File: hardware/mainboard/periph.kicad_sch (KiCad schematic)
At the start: 88 parts, among them J1 Micro_SD_Card_Det, P1 M2_SOCKET_E, Q1 BSS138, Q2 BSS138, Q3 BSS138, Q5 BSS138, Q7 BSS138, SW2 SW_Push, SW3 SW_Push, SW4 SW_Push, SW5 SW_Push, SW6 SW_Push, U10 MMC5983MA, U11 Si52112-B, U21 74LVC2T45DC, U8 TXS02612, U9 ICM-20789, Y1 25MHz

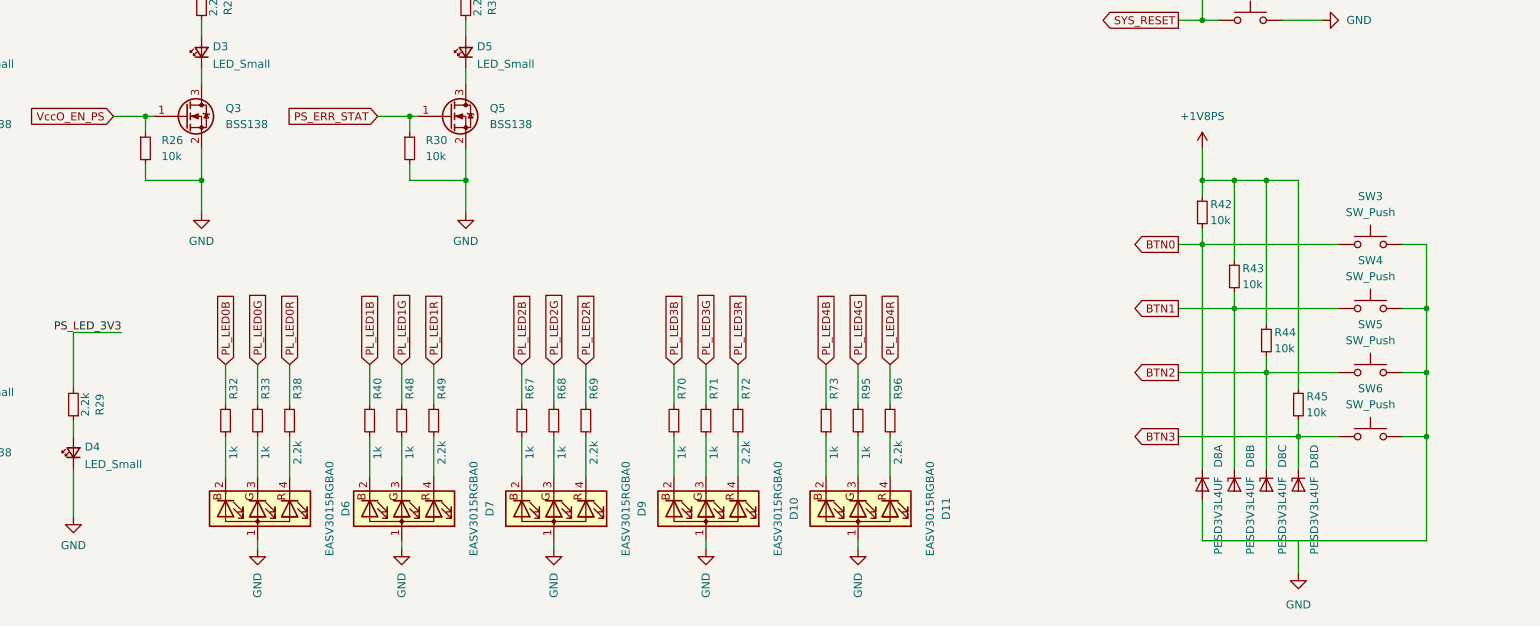
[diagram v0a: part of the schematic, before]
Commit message: Routing various remaining bits
Signed-off-by: gatecat <gatecat@ds0.me>
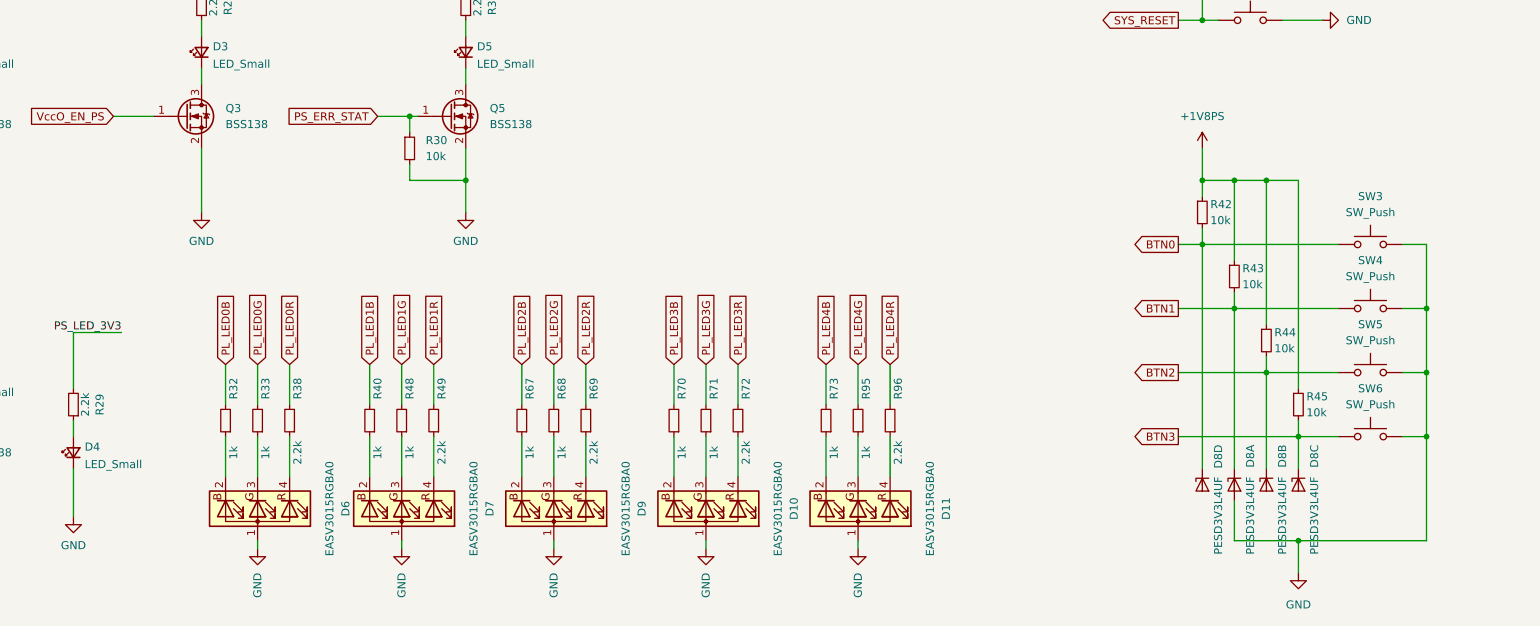
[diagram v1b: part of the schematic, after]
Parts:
- removed R26: 10k, Resistor_SMD:R_0402_1005Metric, symbol Device:R_Small
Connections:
- net BTN0: now also D8.6 (K4); no longer D8.1 (K1)
- net BTN1: now also D8.1 (K1); no longer D8.3 (K2)
- net BTN2: now also D8.3 (K2); no longer D8.4 (K3)
- net BTN3: now also D8.4 (K3); no longer D8.6 (K4)
- net GND: now also D8.2 (A), D8.5 (A), SW3.2, SW4.2, SW5.2, SW6.2
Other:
- moved on the sheet: D8A, D8B, D8C, D8D
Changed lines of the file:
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@@
   (junction (at 218.44 109.22) (diameter 0) (color 0 0 0 0)
   )
-  (junction (at 86.36 215.9) (diameter 0) (color 0 0 0 0)
-  )
   (junction (at 69.85 113.03) (diameter 0) (color 0 0 0 0)
   )
+  (junction (at 260.35 273.05) (diameter 0) (color 0 0 0 0)
+  )
   (junction (at 36.83 257.81) (diameter 0) (color 0 0 0 0)
   )
@@
   (junction (at 226.06 140.97) (diameter 0) (color 0 0 0 0)
   )
-  (junction (at 77.47 205.74) (diameter 0) (color 0 0 0 0)
-  )
   (junction (at 337.82 152.4) (diameter 0) (color 0 0 0 0)
   )
@@
     (stroke (width 0) (type default) (color 0 0 0 0))
   )
+  (wire (pts (xy 250.19 273.05) (xy 260.35 273.05))
+    (stroke (width 0) (type default) (color 0 0 0 0))
+  )
   (wire (pts (xy 140.97 114.3) (xy 140.97 116.84))
     (stroke (width 0) (type default) (color 0 0 0 0))
@@
     (stroke (width 0) (type default) (color 0 0 0 0))
   )
-  (wire (pts (xy 86.36 215.9) (xy 86.36 220.98))
+  (wire (pts (xy 86.36 210.82) (xy 86.36 220.98))
     (stroke (width 0) (type default) (color 0 0 0 0))
   )
@@
     (stroke (width 0) (type default) (color 0 0 0 0))
   )
-  (wire (pts (xy 260.35 273.05) (xy 260.35 278.13))
-    (stroke (width 0) (type default) (color 0 0 0 0))
-  )
   (wire (pts (xy 69.85 78.74) (xy 77.47 78.74))
     (stroke (width 0) (type default) (color 0 0 0 0))
@@
     (stroke (width 0) (type default) (color 0 0 0 0))
   )
-  (wire (pts (xy 77.47 208.28) (xy 77.47 205.74))
-    (stroke (width 0) (type default) (color 0 0 0 0))
-  )
   (wire (pts (xy 241.3 129.54) (xy 241.3 127))
     (stroke (width 0) (type default) (color 0 0 0 0))
@@
     (stroke (width 0) (type default) (color 0 0 0 0))
   )
-  (wire (pts (xy 245.11 266.7) (xy 245.11 273.05))
-    (stroke (width 0) (type default) (color 0 0 0 0))
-  )
   (wire (pts (xy 280.67 273.05) (xy 280.67 256.54))
     (stroke (width 0) (type default) (color 0 0 0 0))
@@
     (stroke (width 0) (type default) (color 0 0 0 0))
   )
-  (wire (pts (xy 72.39 205.74) (xy 77.47 205.74))
+  (wire (pts (xy 72.39 205.74) (xy 78.74 205.74))
     (stroke (width 0) (type default) (color 0 0 0 0))
   )
@@
     (stroke (width 0) (type default) (color 0 0 0 0))
   )
-  (wire (pts (xy 86.36 215.9) (xy 77.47 215.9))
-    (stroke (width 0) (type default) (color 0 0 0 0))
-  )
   (wire (pts (xy 306.07 142.24) (xy 309.88 142.24))
     (stroke (width 0) (type default) (color 0 0 0 0))
@@
     (stroke (width 0) (type default) (color 0 0 0 0))
   )
-  (wire (pts (xy 245.11 273.05) (xy 280.67 273.05))
-    (stroke (width 0) (type default) (color 0 0 0 0))
-  )
   (wire (pts (xy 314.96 139.7) (xy 340.36 139.7))
     (stroke (width 0) (type default) (color 0 0 0 0))
@@
     (stroke (width 0) (type default) (color 0 0 0 0))
   )
-  (wire (pts (xy 118.11 45.72) (xy 140.97 45.72))
+  (wire (pts (xy 260.35 273.05) (xy 260.35 278.13))
     (stroke (width 0) (type default) (color 0 0 0 0))
   )
-  (wire (pts (xy 77.47 215.9) (xy 77.47 213.36))
+  (wire (pts (xy 118.11 45.72) (xy 140.97 45.72))
     (stroke (width 0) (type default) (color 0 0 0 0))
   )
@@
     (stroke (width 0) (type default) (color 0 0 0 0))
   )
+  (wire (pts (xy 260.35 273.05) (xy 280.67 273.05))
+    (stroke (width 0) (type default) (color 0 0 0 0))
+  )
   (wire (pts (xy 299.72 208.28) (xy 313.69 208.28))
     (stroke (width 0) (type default) (color 0 0 0 0))
@@
     (stroke (width 0) (type default) (color 0 0 0 0))
   )
+  (wire (pts (xy 250.19 266.7) (xy 250.19 273.05))
+    (stroke (width 0) (type default) (color 0 0 0 0))
+  )
   (wire (pts (xy 118.11 43.18) (xy 140.97 43.18))
     (stroke (width 0) (type default) (color 0 0 0 0))
@@
     (stroke (width 0) (type default) (color 0 0 0 0))
   )
-  (wire (pts (xy 86.36 210.82) (xy 86.36 215.9))
-    (stroke (width 0) (type default) (color 0 0 0 0))
-  )
   (wire (pts (xy 323.85 223.52) (xy 323.85 226.06))
     (stroke (width 0) (type default) (color 0 0 0 0))
@@
     (stroke (width 0) (type default) (color 0 0 0 0))
   )
-  (wire (pts (xy 77.47 205.74) (xy 78.74 205.74))
-    (stroke (width 0) (type default) (color 0 0 0 0))
-  )
   (wire (pts (xy 241.3 226.06) (xy 245.11 226.06))
     (stroke (width 0) (type default) (color 0 0 0 0))
@@
     (pin "2")
   )
-  (symbol (lib_id "Power_Protection:PESD3V3L4UF") (at 260.35 264.16 270) (unit 4)
+  (symbol (lib_id "Power_Protection:PESD3V3L4UF") (at 245.11 264.16 270) (unit 4)
     (in_bom yes) (on_board yes)
-    (property "Reference" "D8" (id 0) (at 262.89 257.81 0)
+    (property "Reference" "D8" (id 0) (at 247.65 257.81 0)
       (effects (font (size 1.27 1.27)) (justify left))
     )
-    (property "Value" "PESD3V3L4UF" (id 1) (at 262.89 262.89 0)
+    (property "Value" "PESD3V3L4UF" (id 1) (at 247.65 262.89 0)
       (effects (font (size 1.27 1.27)) (justify left))
     )
-    (property "Footprint" "Package_TO_SOT_SMD:SOT-886" (id 2) (at 260.35 264.16 0)
+    (property "Footprint" "Package_TO_SOT_SMD:SOT-886" (id 2) (at 245.11 264.16 0)
       (effects (font (size 1.27 1.27)) hide)
     )
-    (property "Datasheet" "https://assets.nexperia.com/documents/data-sheet/PESDXL4UF_G_W.pdf" (id 3) (at 260.35 264.16 0)
+    (property "Datasheet" "https://assets.nexperia.com/documents/data-sheet/PESDXL4UF_G_W.pdf" (id 3) (at 245.11 264.16 0)
       (effects (font (size 1.27 1.27)) hide)
     )
@@
     (pin "1")
   )
-  (symbol (lib_id "Power_Protection:PESD3V3L4UF") (at 245.11 264.16 270) (unit 1)
+  (symbol (lib_id "Power_Protection:PESD3V3L4UF") (at 250.19 264.16 270) (unit 1)
     (in_bom yes) (on_board yes)
-    (property "Reference" "D8" (id 0) (at 247.65 257.81 0)
+    (property "Reference" "D8" (id 0) (at 252.73 257.81 0)
       (effects (font (size 1.27 1.27)) (justify left))
     )
-    (property "Value" "PESD3V3L4UF" (id 1) (at 247.65 262.89 0)
+    (property "Value" "PESD3V3L4UF" (id 1) (at 252.73 262.89 0)
       (effects (font (size 1.27 1.27)) (justify left))
     )
-    (property "Footprint" "Package_TO_SOT_SMD:SOT-886" (id 2) (at 245.11 264.16 0)
+    (property "Footprint" "Package_TO_SOT_SMD:SOT-886" (id 2) (at 250.19 264.16 0)
       (effects (font (size 1.27 1.27)) hide)
     )
-    (property "Datasheet" "https://assets.nexperia.com/documents/data-sheet/PESDXL4UF_G_W.pdf" (id 3) (at 245.11 264.16 0)
+    (property "Datasheet" "https://assets.nexperia.com/documents/data-sheet/PESDXL4UF_G_W.pdf" (id 3) (at 250.19 264.16 0)
       (effects (font (size 1.27 1.27)) hide)
     )
@@
     (pin "1")
   )
-  (symbol (lib_id "Device:R_Small") (at 77.47 210.82 0) (unit 1)
-    (in_bom yes) (on_board yes) (fields_autoplaced)
-    (property "Reference" "R26" (id 0) (at 80.01 209.5499 0)
-      (effects (font (size 1.27 1.27)) (justify left))
-    )
-    (property "Value" "10k" (id 1) (at 80.01 212.0899 0)
-      (effects (font (size 1.27 1.27)) (justify left))
-    )
-    (property "Footprint" "Resistor_SMD:R_0402_1005Metric" (id 2) (at 77.47 210.82 0)
-      (effects (font (size 1.27 1.27)) hide)
-    )
-    (property "Datasheet" "~" (id 3) (at 77.47 210.82 0)
-      (effects (font (size 1.27 1.27)) hide)
-    )
-    (pin "1")
-    (pin "2")
-  )
   (symbol (lib_id "Device:R_Small") (at 312.42 116.84 90) (unit 1)
     (in_bom yes) (on_board yes)
@@
     (pin "2")
   )
-  (symbol (lib_id "Power_Protection:PESD3V3L4UF") (at 250.19 264.16 270) (unit 2)
+  (symbol (lib_id "Power_Protection:PESD3V3L4UF") (at 255.27 264.16 270) (unit 2)
     (in_bom yes) (on_board yes)
-    (property "Reference" "D8" (id 0) (at 252.73 257.81 0)
+    (property "Reference" "D8" (id 0) (at 257.81 257.81 0)
       (effects (font (size 1.27 1.27)) (justify left))
     )
-    (property "Value" "PESD3V3L4UF" (id 1) (at 252.73 262.89 0)
+    (property "Value" "PESD3V3L4UF" (id 1) (at 257.81 262.89 0)
       (effects (font (size 1.27 1.27)) (justify left))
     )
-    (property "Footprint" "Package_TO_SOT_SMD:SOT-886" (id 2) (at 250.19 264.16 0)
+    (property "Footprint" "Package_TO_SOT_SMD:SOT-886" (id 2) (at 255.27 264.16 0)
       (effects (font (size 1.27 1.27)) hide)
     )
-    (property "Datasheet" "https://assets.nexperia.com/documents/data-sheet/PESDXL4UF_G_W.pdf" (id 3) (at 250.19 264.16 0)
+    (property "Datasheet" "https://assets.nexperia.com/documents/data-sheet/PESDXL4UF_G_W.pdf" (id 3) (at 255.27 264.16 0)
       (effects (font (size 1.27 1.27)) hide)
     )
@@
     (pin "1")
   )
-  (symbol (lib_id "Power_Protection:PESD3V3L4UF") (at 255.27 264.16 270) (unit 3)
+  (symbol (lib_id "Power_Protection:PESD3V3L4UF") (at 260.35 264.16 270) (unit 3)
     (in_bom yes) (on_board yes)
-    (property "Reference" "D8" (id 0) (at 257.81 257.81 0)
+    (property "Reference" "D8" (id 0) (at 262.89 257.81 0)
       (effects (font (size 1.27 1.27)) (justify left))
     )
-    (property "Value" "PESD3V3L4UF" (id 1) (at 257.81 262.89 0)
+    (property "Value" "PESD3V3L4UF" (id 1) (at 262.89 262.89 0)
       (effects (font (size 1.27 1.27)) (justify left))
     )
-    (property "Footprint" "Package_TO_SOT_SMD:SOT-886" (id 2) (at 255.27 264.16 0)
+    (property "Footprint" "Package_TO_SOT_SMD:SOT-886" (id 2) (at 260.35 264.16 0)
       (effects (font (size 1.27 1.27)) hide)
     )
-    (property "Datasheet" "https://assets.nexperia.com/documents/data-sheet/PESDXL4UF_G_W.pdf" (id 3) (at 255.27 264.16 0)
+    (property "Datasheet" "https://assets.nexperia.com/documents/data-sheet/PESDXL4UF_G_W.pdf" (id 3) (at 260.35 264.16 0)
       (effects (font (size 1.27 1.27)) hide)
     )
